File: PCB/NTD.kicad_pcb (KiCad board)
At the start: 2 copper layers, 59.3 x 60.8 mm, 10 parts, among them J1 Conn_01x04, SW1 SW_Push, SW2 SW_Push, SW3 SW_Push, SW4 SW_Push, SW5 SW_Push, SW6 SW_Push, U1 XIAO-RP2040-DIP

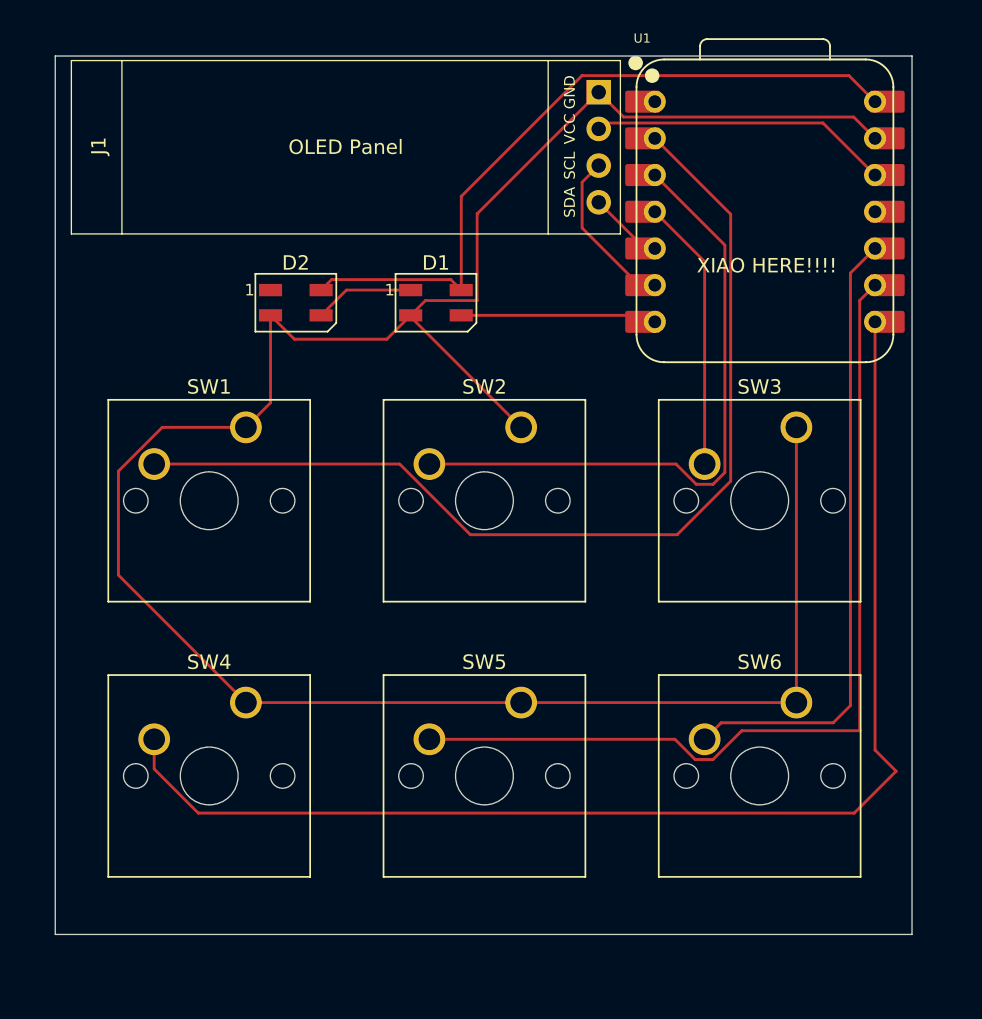
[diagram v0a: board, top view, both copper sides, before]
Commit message: Update print statement from 'Hello' to 'Goodbye'
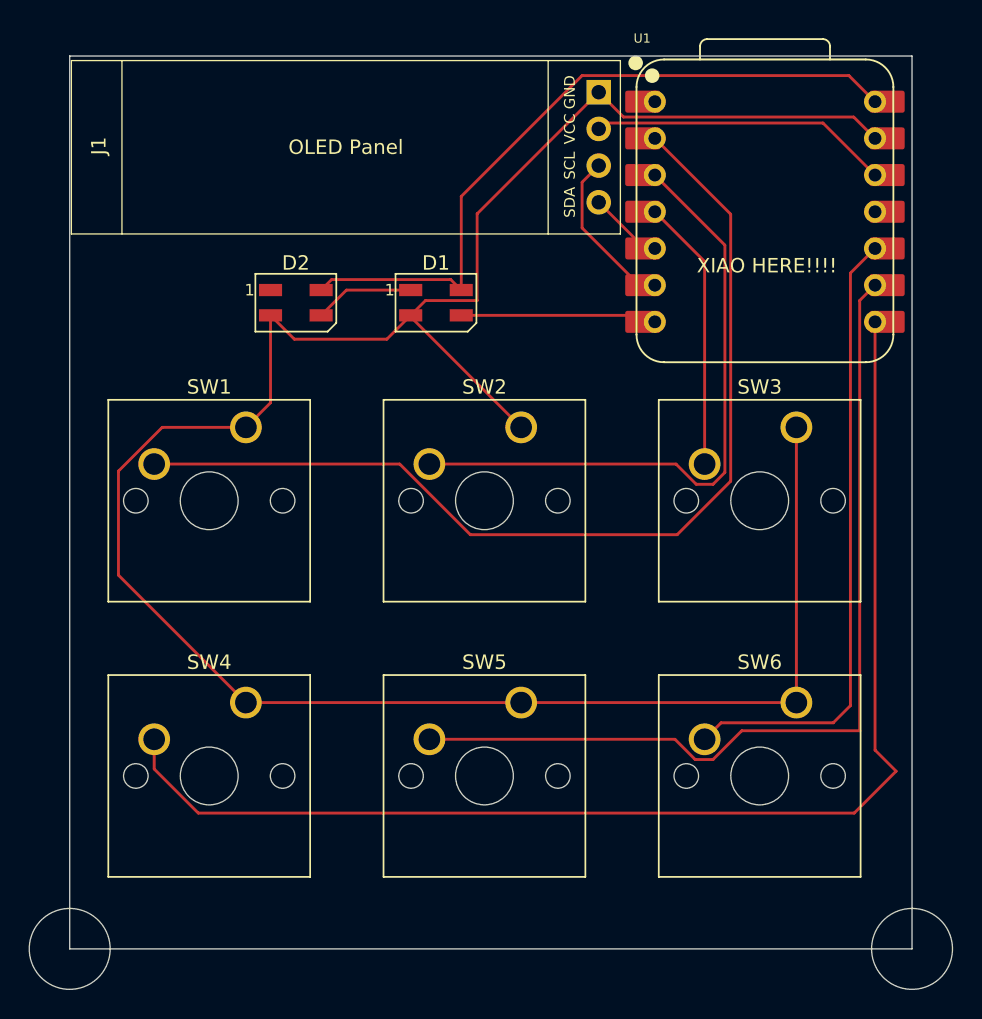
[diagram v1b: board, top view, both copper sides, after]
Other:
- board size 59.3 x 60.8 mm -> 63.9 x 64.6 mm
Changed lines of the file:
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@@
 		)
 	)
-	(gr_rect
-		(start 96.5 85.9)
-		(end 155.8 146.7)
+	(gr_circle
+		(center 97.5 147.7)
+		(end 97.5 150.5)
 		(stroke
 			(width 0.05)
+			(type default)
+		)
+		(fill no)
+		(layer "Edge.Cuts")
+	)
+	(gr_circle
+		(center 155.8 147.7)
+		(end 155.8 150.5)
+		(stroke
+			(width 0.05)
+			(type default)
+		)
+		(fill no)
+		(layer "Edge.Cuts")
+	)
+	(gr_rect
+		(start 97.5 85.9)
+		(end 155.8 147.7)
+		(stroke
+			(width 0.05)

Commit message: r
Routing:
- net Net-(U1-GPIO1/RX): track 87.6 -> 86.4 mm
- net Net-(U1-GPIO2/SCK): track 62.5 -> 61.9 mm
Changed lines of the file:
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@@
 			(outputformat 1)
 			(mirror no)
-			(drillshape 1)
+			(drillshape 0)
 			(scaleselection 1)
-			(outputdirectory "")
+			(outputdirectory "Fabrication/")
 		)
 	)
@@
 	)
 	(segment
-		(start 144.018814 132.6)
-		(end 152.2 132.6)
+		(start 142.026564 134.59225)
+		(end 144.018814 132.6)
 		(width 0.2)
 		(layer "F.Cu")
@@
 	)
 	(segment
-		(start 142.026564 134.59225)
-		(end 144.018814 132.6)
+		(start 150.9 132.6)
+		(end 152.4 131.1)
 		(width 0.2)
 		(layer "F.Cu")
@@
 	)
 	(segment
-		(start 152.177 132.577)
-		(end 152.177 102.823)
+		(start 152.4 131.1)
+		(end 152.177 130.877)
 		(width 0.2)
 		(layer "F.Cu")
@@
 	)
 	(segment
-		(start 152.2 132.6)
-		(end 152.177 132.577)
+		(start 144.018814 132.6)
+		(end 150.9 132.6)
 		(width 0.2)
 		(layer "F.Cu")
@@
 	)
 	(segment
+		(start 152.177 130.877)
+		(end 152.177 102.823)
+		(width 0.2)
+		(layer "F.Cu")
+		(net 6)
+	)
+	(segment
 		(start 122.39625 133.19125)
 		(end 139.391434 133.19125)
@@
 	)
 	(segment
-		(start 153.24 133.94)
-		(end 153.24 104.3)
+		(start 106.400184 138.3)
+		(end 103.34625 135.246066)
 		(width 0.2)
 		(layer "F.Cu")
@@
 	)
 	(segment
-		(start 154.7 135.4)
-		(end 153.24 133.94)
-		(width 0.2)
-		(layer "F.Cu")
-		(net 14)
-	)
-	(segment
-		(start 151.8 138.3)
-		(end 154.7 135.4)
+		(start 153.24 104.3)
+		(end 153.24 136.86)
 		(width 0.2)
 		(layer "F.Cu")
@@
 	(segment
 		(start 103.34625 135.246066)
-		(end 106.400184 138.3)
+		(end 103.34625 133.19125)
 		(width 0.2)
 		(layer "F.Cu")
@@
 	)
 	(segment
-		(start 103.34625 133.19125)
-		(end 103.34625 135.246066)
+		(start 151.8 138.3)
+		(end 106.400184 138.3)
 		(width 0.2)
 		(layer "F.Cu")
@@
 	)
 	(segment
-		(start 106.400184 138.3)
+		(start 153.24 136.86)
 		(end 151.8 138.3)
 		(width 0.2)

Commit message: o
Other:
- board size 63.9 x 64.6 mm -> 58.3 x 61.8 mm
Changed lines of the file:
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@@
 		)
-	)
-	(gr_circle
-		(center 97.5 147.7)
-		(end 97.5 150.5)
-		(stroke
-			(width 0.05)
-			(type default)
-		)
-		(fill no)
-		(layer "Edge.Cuts")
-	)
-	(gr_circle
-		(center 155.8 147.7)
-		(end 155.8 150.5)
-		(stroke
-			(width 0.05)
-			(type default)
-		)
-		(fill no)
-		(layer "Edge.Cuts")
 	)
 	(gr_rect
